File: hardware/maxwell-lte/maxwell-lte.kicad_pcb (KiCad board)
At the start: 2 copper layers, 69 x 39 mm, 25 parts, among them J1 LTE, J2 GPS, J3 Input, J4 SIM_Card, U1 MIC5209-ADJ, U2 SIM7000A, U3 TXB0104D, U4 SC16IS750IPW, Y1 Crystal

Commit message: Rev 1.1.
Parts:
- removed C8, C9: 220u / TAJC227K006RNJ, coddingtonbear:CP_Tantalum_Case-C_EIA-6032-28_Milling
- removed R4, R5, R6: 22, coddingtonbear:0805_Milling
- added D1: 1N4148W, coddingtonbear:D_SOD-123_LargePads, F.Cu at (123.5, 90.5)
- added R7: 1k, coddingtonbear:0805_Milling, F.Cu at (131.2, 82.8)
- added R8: 3.6k, coddingtonbear:0805_Milling, F.Cu at (127.8, 89.5)
- C7: value 220u / TAJC227K006RNJ -> 0.1 / FG0H104ZF; footprint coddingtonbear:CP_Tantalum_Case-C_EIA-6032-28_Milling -> Capacitor_THT:C_Disc_D11.0mm_W5.0mm_P5.00mm; moved to B.Cu
- J1, J2: footprint Connector_Coaxial:SMA_Amphenol_132134_Vertical -> coddingtonbear:SMA_Amphenol_132134_Vertical_Largepads
- U1: footprint Package_SO:SOIC-8_3.9x4.9mm_P1.27mm -> coddingtonbear:SOIC-8_3.9x4.9mm_P1.27mm_LargePads
- U3: footprint Package_SO:SOIC-14_3.9x8.7mm_P1.27mm -> coddingtonbear:SOIC-14_3.9x8.7mm_P1.27mm_LargePads
- U4: footprint Package_SO:TSSOP-24_4.4x7.8mm_P0.65mm -> coddingtonbear:TSSOP-24_4.4x7.8mm_P0.65mm_LargePads
- moved R3 4.21 mm to (131.5, 84.8), turned to 0 degrees
- moved C1 3.38 mm to (118.2, 90.2)
- moved C7 2.67 mm to (96.0, 96.0)
- moved C10 1.30 mm to (129.8, 74.0)
- moved C6 0.25 mm to (99.1, 73.8)
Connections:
- C1 pad 1: /VDD_EXT -> +1V8
- U2 pad 15: /VDD_EXT -> +1V8
- U2 pad 31: Net-(R4-Pad2) -> Net-(J4-Pad7)
- U2 pad 32: Net-(R6-Pad2) -> Net-(J4-Pad3)
- U2 pad 33: Net-(R5-Pad2) -> Net-(J4-Pad2)
- U3 pad 1: /VDD_EXT -> +1V8
- U3 pad 8: /VDD_EXT -> EN_OUTPUT
- U4 pad 21: (no net) -> EN_OUTPUT
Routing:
- net Net-(J4-Pad7): track 19.8 -> 53.5 mm
- net EN_OUTPUT: track 0.00 -> 25.1 mm
- net Net-(R4-Pad2): track 23.0 -> 0.00 mm
- net /VDD_EXT: track 22.1 -> 0.00 mm
- net GND: track 164.8 -> 185.9 mm, vias 24 -> 27
- net Net-(D1-Pad2): track 0.00 -> 11.1 mm
- net +BATT: track 168.9 -> 158.2 mm
- net +1V8: track 0.00 -> 10.3 mm
- net Net-(R5-Pad2): track 5.57 -> 0.00 mm
- net Net-(J4-Pad3): track 11.1 -> 15.7 mm
- net /LTE_ANT: track 4.24 -> 0.00 mm
- net Net-(R6-Pad2): track 3.40 -> 0.00 mm
- net CS: track 38.3 -> 35.8 mm
- net +3V3: track 86.1 -> 88.5 mm
- net Net-(R3-Pad1): track 3.40 -> 5.78 mm
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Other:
- board text added: "Maxwell-LTE v1.1"
- board text removed: "Maxwell-LTE v1"

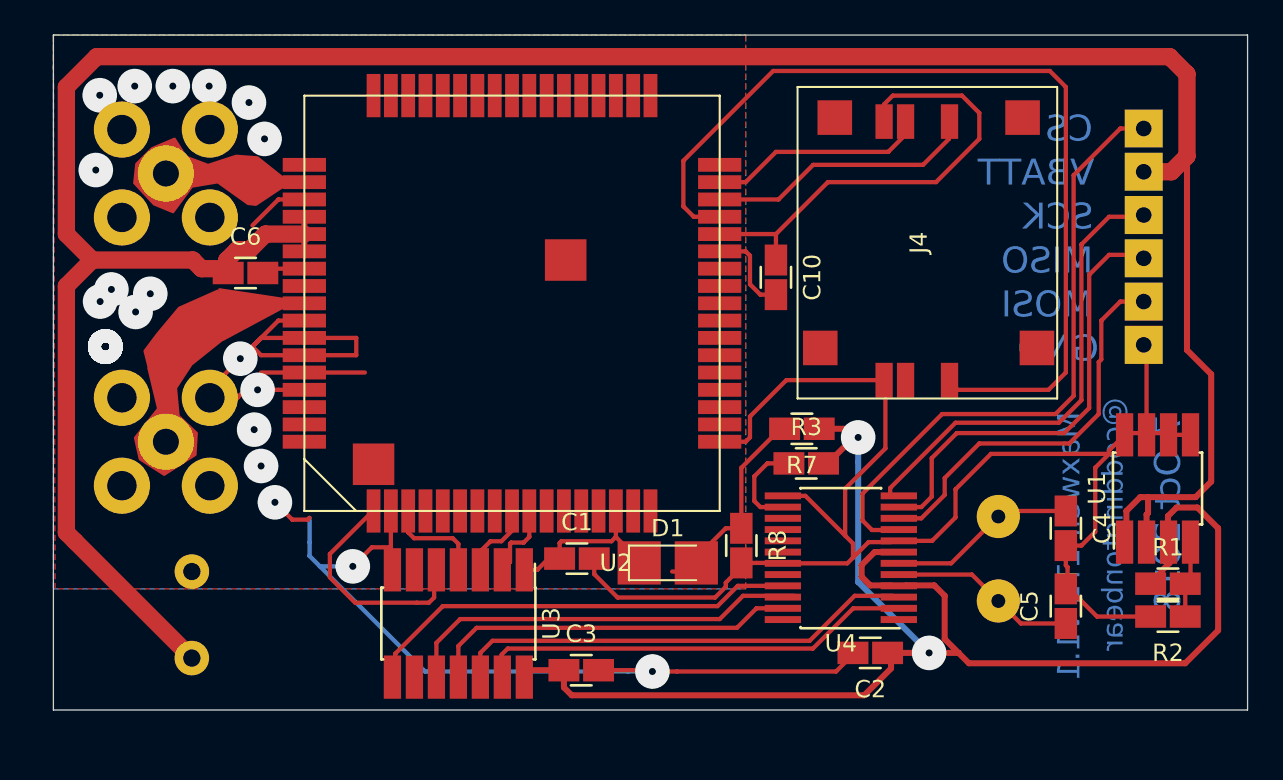
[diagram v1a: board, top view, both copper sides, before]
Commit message: Adding similarly-enormous GND trace.
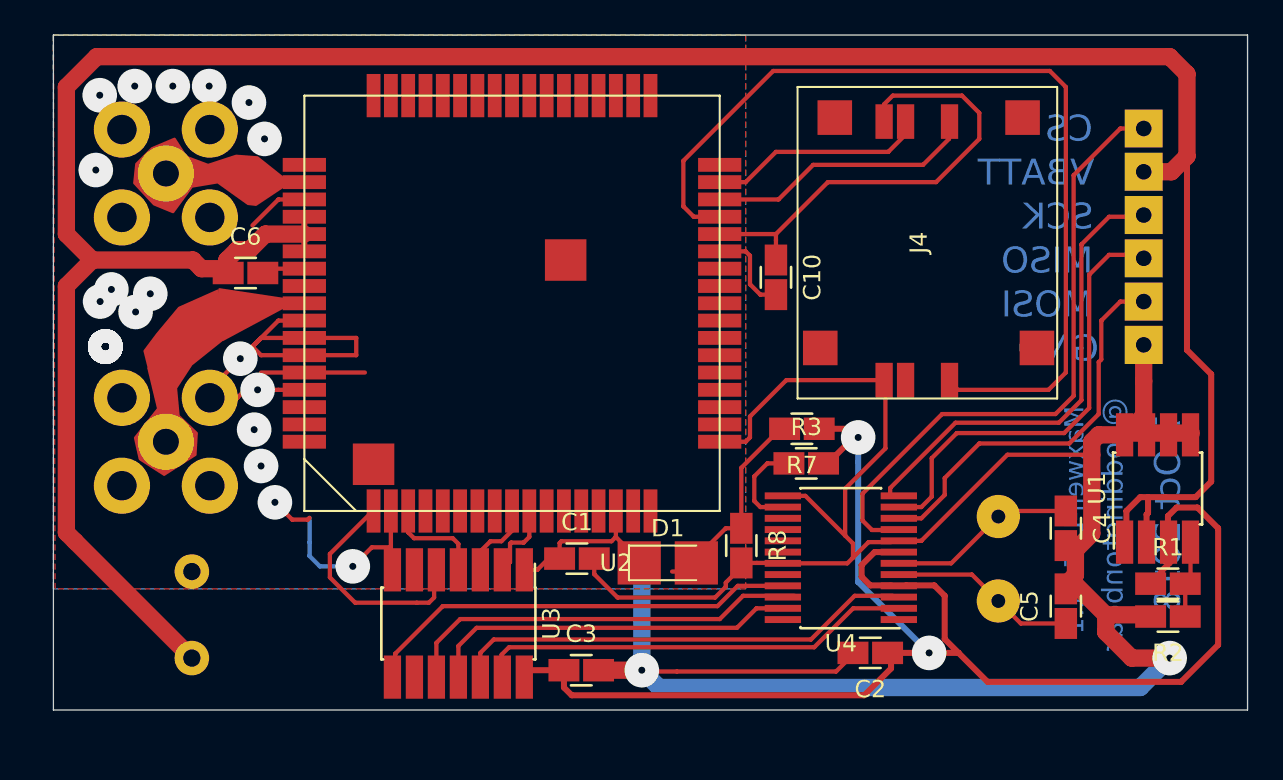
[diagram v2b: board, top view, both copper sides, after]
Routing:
- net GND: track 185.9 -> 205.7 mm, vias 27 -> 28
- net +3V3: track 88.5 -> 89.9 mm

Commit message: Adding similarly-enormous GND trace.
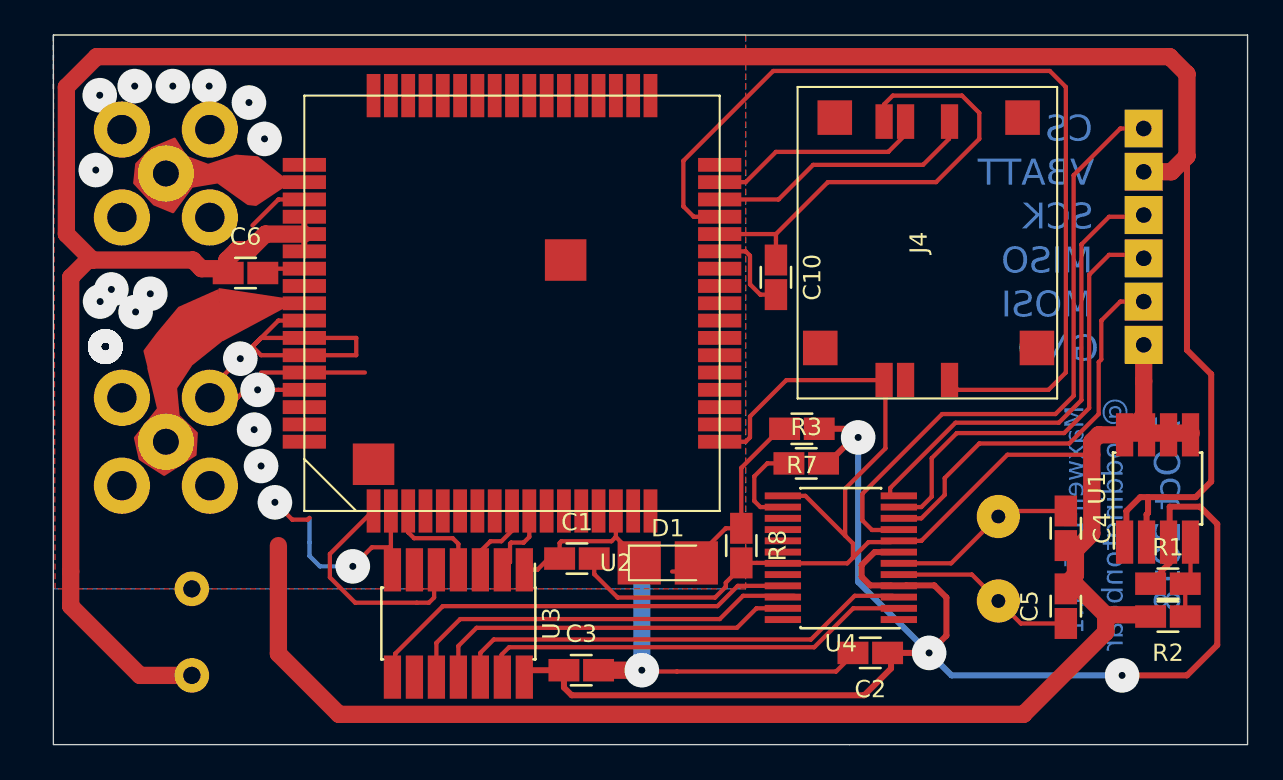
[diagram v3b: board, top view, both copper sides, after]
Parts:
- moved C7 1.00 mm to (96.0, 97.0)
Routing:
- net GND: track 205.7 -> 227.2 mm, vias 28 -> 27
- net +BATT: track 158.2 -> 160.9 mm
- net +3V3: track 89.9 -> 90.9 mm, vias 2 -> 3
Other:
- board size 69 x 39 mm -> 69 x 41 mm
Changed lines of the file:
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@@
   (general
     (thickness 1.6)
-    (drawings 17)
+    (drawings 20)
     (tracks 360)
     (zones 0)
@@
     (pad_to_mask_clearance 0.051)
     (solder_mask_min_width 0.25)
-    (aux_axis_origin 88 99)
+    (aux_axis_origin 88 101)
     (visible_elements FFFFFF7F)
     (pcbplotparams
@@
   )
   (module Capacitor_THT:C_Disc_D11.0mm_W5.0mm_P5.00mm (layer B.Cu)
-    (at 96 96 90)
+    (at 96 97 90)
     (descr "C, Disc series, Radial, pin pitch=5.00mm, , diameter*width=11*5.0mm^2, Capacitor, http://www.vishay.com/docs/28535/vy2series.pdf")
     (tags "C Disc series Radial pin pitch 5.00mm  diameter 11mm width 5.0mm Capacitor")
@@
     )
   )
+  (gr_line (start 88 101) (end 88 99) (layer Edge.Cuts) (width 0.05))
+  (gr_line (start 134 101) (end 88 101) (layer Edge.Cuts) (width 0.05))
+  (gr_line (start 157 101) (end 134 101) (layer Edge.Cuts) (width 0.05))
+  (gr_line (start 157 99) (end 157 101) (layer Edge.Cuts) (width 0.05))
   (gr_poly (pts (xy 95.925 79.1) (xy 97.8 77.6) (xy 97.5 74.75) (xy 95.25 75.75) (xy 94 77.25) (xy 93.25 78.25) (xy 93.5 79.25)) (layer F.Cu) (width 0.1))
   (gr_text "7 Oct 2018" (at 152.4 87.63 90) (layer B.Cu)
@@
     (effects (font (size 1.5 1.5) (thickness 0.3)) (justify mirror))
   )
-  (gr_line (start 88 99) (end 157 99) (layer Edge.Cuts) (width 0.05))
   (gr_line (start 88 60) (end 88 99) (layer Edge.Cuts) (width 0.05))
   (gr_line (start 157 60) (end 88 60) (layer Edge.Cuts) (width 0.05))
@@
   (via (at 122 96.7) (size 2) (drill 0.4) (layers F.Cu B.Cu) (net 1))
   (segment (start 122 96.7) (end 122 90) (width 1) (layer B.Cu) (net 1))
-  (via (at 152.5 96) (size 2) (drill 0.4) (layers F.Cu B.Cu) (net 1))
-  (segment (start 150.305002 96) (end 152.5 96) (width 1) (layer F.Cu) (net 1))
+  (segment (start 148.805002 94.5) (end 144.055002 99.25) (width 1) (layer F.Cu) (net 1))
   (segment (start 148.805002 93.5) (end 148.805002 94.5) (width 1) (layer F.Cu) (net 1))
-  (segment (start 148.805002 94.5) (end 150.305002 96) (width 1) (layer F.Cu) (net 1))
-  (segment (start 122.999999 97.699999) (end 122 96.7) (width 1) (layer B.Cu) (net 1))
-  (segment (start 150.800001 97.699999) (end 122.999999 97.699999) (width 1) (layer B.Cu) (net 1))
-  (segment (start 152.5 96) (end 150.800001 97.699999) (width 1) (layer B.Cu) (net 1))
-  (segment (start 137.25 91.825) (end 137.275 91.8) (width 0.35) (layer F.Cu) (net 2))
-  (segment (start 136.35 91.825) (end 137.25 91.825) (width 0.35) (layer F.Cu) (net 2))
-  (segment (start 137.275 91.8) (end 138.9 91.8) (width 0.35) (layer F.Cu) (net 2))
-  (segment (start 138.9 91.8) (end 139.5 92.4) (width 0.35) (layer F.Cu) (net 2))
-  (segment (start 139.5 92.4) (end 139.5 94.9) (width 0.35) (layer F.Cu) (net 2))
-  (segment (start 139.5 94.9) (end 140.3 95.7) (width 0.35) (layer F.Cu) (net 2))
+  (segment (start 144.055002 99.25) (end 104.5 99.25) (width 1) (layer F.Cu) (net 1))
+  (segment (start 104.5 99.25) (end 101 95.75) (width 1) (layer F.Cu) (net 1))
+  (segment (start 101 95.75) (end 101 89.5) (width 1) (layer F.Cu) (net 1))
   (segment (start 117.5 96.7) (end 115.3 96.7) (width 0.35) (layer F.Cu) (net 2))
   (segment (start 135.45 89.875) (end 134.7 90.625) (width 0.35) (layer F.Cu) (net 2))
@@
   (segment (start 138 95.7) (end 138.6 95.7) (width 0.35) (layer F.Cu) (net 2))
   (segment (start 136.2 95.7) (end 138 95.7) (width 0.35) (layer F.Cu) (net 2))
-  (segment (start 138.6 95.7) (end 140.3 95.7) (width 0.35) (layer F.Cu) (net 2))
   (via (at 138.6 95.7) (size 2) (drill 0.4) (layers F.Cu B.Cu) (net 2))
   (segment (start 117.5 96.7) (end 117.5 97.7) (width 0.35) (layer F.Cu) (net 2))
@@
   (segment (start 134.000004 82.75) (end 134.500004 83.25) (width 0.35) (layer F.Cu) (net 2))
   (segment (start 132.25 82.75) (end 134.000004 82.75) (width 0.35) (layer F.Cu) (net 2))
-  (segment (start 141.975002 97.375002) (end 153.160002 97.375002) (width 0.35) (layer F.Cu) (net 2))
-  (segment (start 155.3 95.235004) (end 155.3 88.5) (width 0.35) (layer F.Cu) (net 2))
-  (segment (start 152.9 87.3) (end 152.4 87.8) (width 0.35) (layer F.Cu) (net 2))
-  (segment (start 155.3 88.5) (end 154.1 87.3) (width 0.35) (layer F.Cu) (net 2))
-  (segment (start 152.4 87.8) (end 152.4 88.9) (width 0.35) (layer F.Cu) (net 2))
-  (segment (start 154.1 87.3) (end 152.9 87.3) (width 0.35) (layer F.Cu) (net 2))
-  (segment (start 153.160002 97.375002) (end 155.3 95.235004) (width 0.35) (layer F.Cu) (net 2))
-  (segment (start 140.3 95.7) (end 141.975002 97.375002) (width 0.35) (layer F.Cu) (net 2))
+  (via (at 149.75 97) (size 2) (drill 0.4) (layers F.Cu B.Cu) (net 2))
+  (segment (start 138.6 95.7) (end 139.9 97) (width 0.35) (layer B.Cu) (net 2))
+  (segment (start 139.9 97) (end 149.75 97) (width 0.35) (layer B.Cu) (net 2))
+  (segment (start 149.75 97) (end 153.5 97) (width 0.35) (layer F.Cu) (net 2))
+  (segment (start 153.5 97) (end 155.25 95.25) (width 0.35) (layer F.Cu) (net 2))
+  (segment (start 155.25 95.25) (end 155.25 88.25) (width 0.35) (layer F.Cu) (net 2))
+  (segment (start 155.25 88.25) (end 154.25 87.25) (width 0.35) (layer F.Cu) (net 2))
+  (segment (start 154.25 87.25) (end 152.5 87.25) (width 0.35) (layer F.Cu) (net 2))
+  (segment (start 152.5 87.25) (end 152.5 89.75) (width 0.35) (layer F.Cu) (net 2))
+  (segment (start 137.275 91.8) (end 137.25 91.825) (width 0.35) (layer F.Cu) (net 2))
+  (segment (start 138.9 91.8) (end 137.275 91.8) (width 0.35) (layer F.Cu) (net 2))
+  (segment (start 139.599999 92.499999) (end 138.9 91.8) (width 0.35) (layer F.Cu) (net 2))
+  (segment (start 139.599999 94.700001) (end 139.599999 92.499999) (width 0.35) (layer F.Cu) (net 2))
+  (segment (start 137.25 91.825) (end 136.35 91.825) (width 0.35) (layer F.Cu) (net 2))
+  (segment (start 138.6 95.7) (end 139.599999 94.700001) (width 0.35) (layer F.Cu) (net 2))
   (segment (start 136.35 90.525) (end 139.875 90.525) (width 0.25) (layer F.Cu) (net 3))
   (segment (start 139.875 90.525) (end 142.5 87.9) (width 0.25) (layer F.Cu) (net 3))
@@
   (segment (start 153.5 62.25) (end 153.5 67) (width 1) (layer F.Cu) (net 6))
   (segment (start 151 67.9) (end 152.6 67.9) (width 1) (layer F.Cu) (net 6))
-  (segment (start 90.25 73) (end 88.75 74.5) (width 1) (layer F.Cu) (net 6))
-  (segment (start 89.25 89.25) (end 96 96) (width 1) (layer F.Cu) (net 6))
   (segment (start 150.8 86.7) (end 150 87.5) (width 0.35) (layer F.Cu) (net 6))
   (segment (start 150 87.5) (end 150 89.75) (width 0.35) (layer F.Cu) (net 6))
@@
   (segment (start 151.165 89.3) (end 151.165 87.7) (width 0.35) (layer F.Cu) (net 6))
   (segment (start 151.25 86.7) (end 150.8 86.7) (width 0.35) (layer F.Cu) (net 6))
-  (segment (start 88.75 74.5) (end 88.75 88.75) (width 1) (layer F.Cu) (net 6))
-  (segment (start 88.75 88.75) (end 89.25 89.25) (width 1) (layer F.Cu) (net 6))
   (segment (start 149 70.5) (end 151.1 70.5) (width 0.25) (layer F.Cu) (net 7))
   (segment (start 147.400022 72.099978) (end 149 70.5) (width 0.25) (layer F.Cu) (net 7))
@@
   (segment (start 134.75 86.5) (end 134.75 88.05) (width 0.25) (layer F.Cu) (net 5))
   (segment (start 139.35 81.9) (end 134.75 86.5) (width 0.25) (layer F.Cu) (net 5))
+  (segment (start 90.25 73) (end 90 73) (width 1) (layer F.Cu) (net 6))
+  (segment (start 90 73) (end 89 74) (width 1) (layer F.Cu) (net 6))
+  (segment (start 89 74) (end 89 91) (width 1) (layer F.Cu) (net 6))
+  (segment (start 89 91) (end 89 93) (width 1) (layer F.Cu) (net 6))
+  (segment (start 89 93) (end 93 97) (width 1) (layer F.Cu) (net 6))
+  (segment (start 93 97) (end 96 97) (width 1) (layer F.Cu) (net 6))
   (segment (start 113.9 95.8) (end 113.9 96.8) (width 0.25) (layer F.Cu) (net 15))
   (segment (start 114.325002 95.374998) (end 113.9 95.8) (width 0.25) (layer F.Cu) (net 15))
